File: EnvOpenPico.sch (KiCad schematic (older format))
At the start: 37 parts, among them J2 Conn_01x02, J3 Conn_02x18_Odd_Even, J4 Conn_02x18_Odd_Even, J5 Conn_01x03_Male, U1 SPX3819M5-L-3-3, U2 W25Q256JVEIQ, U3 RP2040, X1 XO32

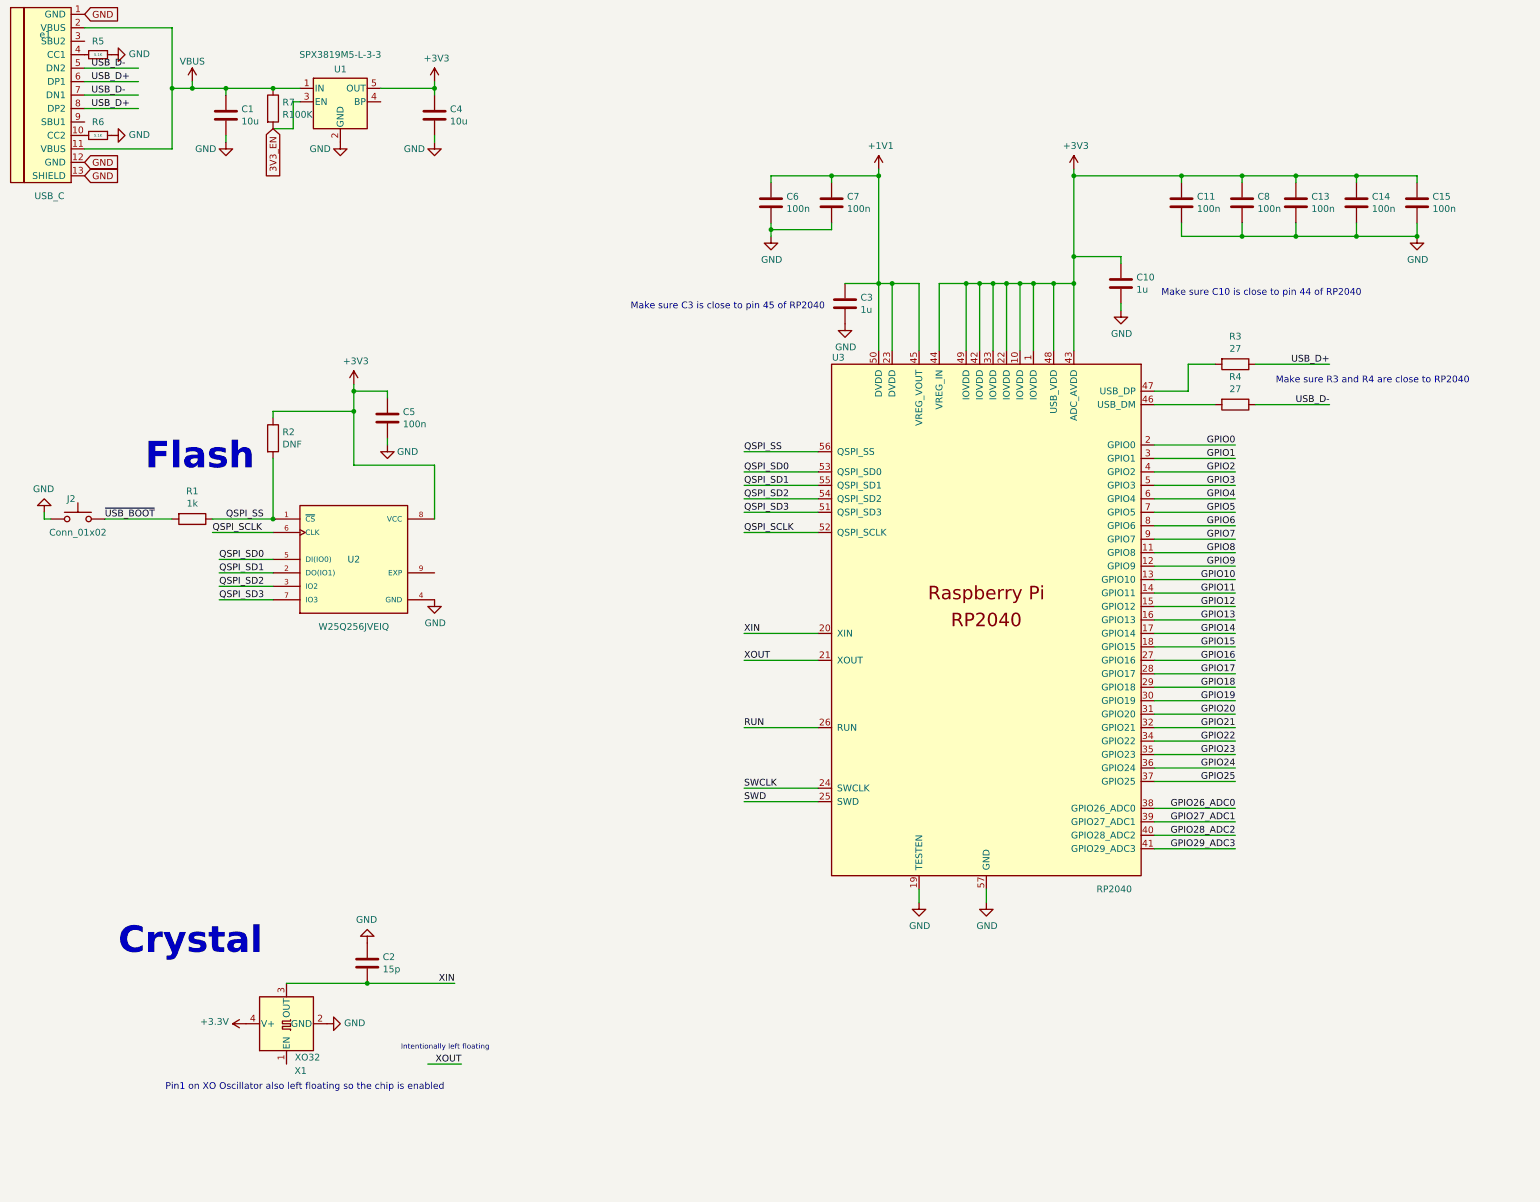
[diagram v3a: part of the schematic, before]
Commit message: Added a Bunch of notes and useful info to the schematic
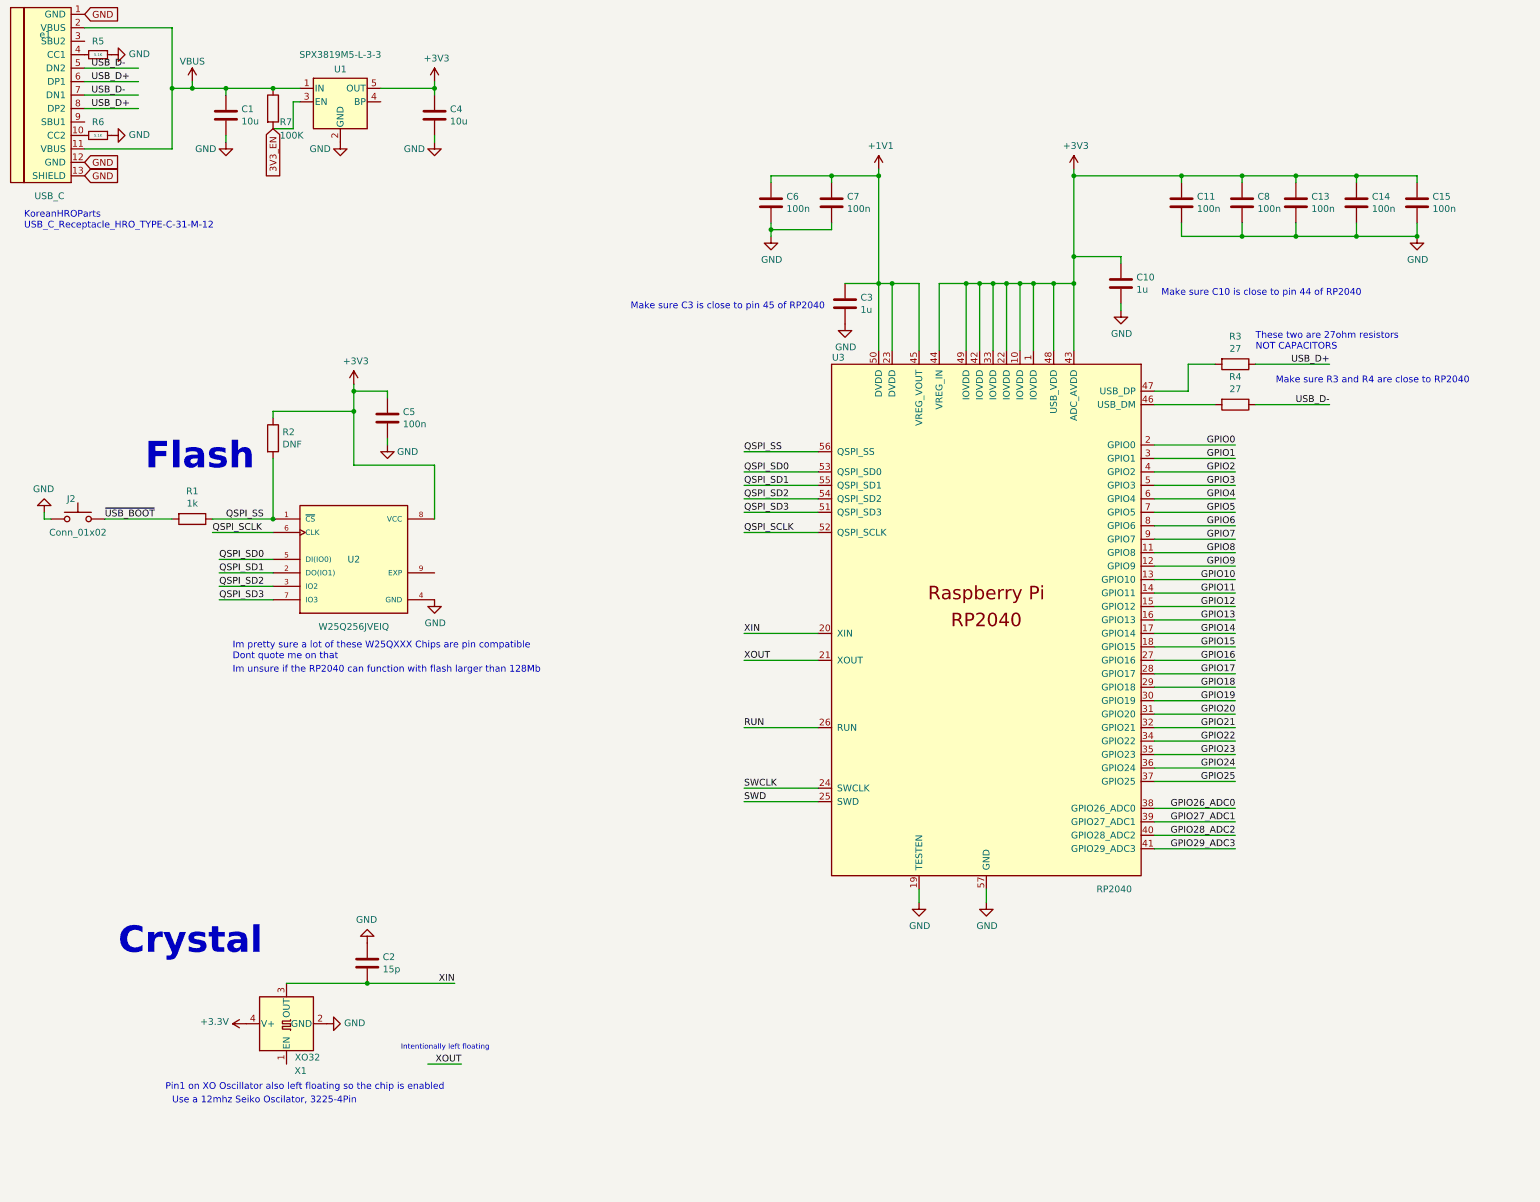
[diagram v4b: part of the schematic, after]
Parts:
- R7: value R100K -> 100K
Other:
- note added: "Im pretty sure a lot of these W25QXXX Chips are pin compatible\nDont quote me on that"
- note added: "Im unsure if the RP2040 can function with flash larger than 128Mb"
- note added: "KoreanHROParts \nUSB_C_Receptacle_HRO_TYPE-C-31-M-12"
- note added: "These two are 27ohm resistors \nNOT CAPACITORS"
- note added: "Use a 12mhz Seiko Oscilator, 3225-4Pin"
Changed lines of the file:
@@
 U 1 1 608CFAF0
 P 2500 1900
-F 0 "R7" H 2570 1946 50  0000 L CNN
-F 1 "R100K" H 2570 1855 50  0000 L CNN
+F 0 "R7" H 2550 1800 50  0000 L CNN
+F 1 "100K" H 2550 1700 50  0000 L CNN
 F 2 "Resistor_SMD:R_0402_1005Metric" V 2430 1900 50  0001 C CNN
 F 3 "~" H 2500 1900 50  0001 C CNN
@@
 	1    0    0    -1
 $EndComp
+Text Notes 1750 9300 0    50   ~ 0
+Use a 12mhz Seiko Oscilator, 3225-4Pin
+Text Notes 2200 6000 0    50   ~ 0
+Im pretty sure a lot of these W25QXXX Chips are pin compatible\nDont quote me on that
+Text Notes 9800 3700 0    50   ~ 0
+These two are 27ohm resistors \nNOT CAPACITORS
+Text Notes 650  2800 0    50   ~ 0
+KoreanHROParts \nUSB_C_Receptacle_HRO_TYPE-C-31-M-12
+Text Notes 2200 6100 0    50   ~ 0
+Im unsure if the RP2040 can function with flash larger than 128Mb
 $EndSCHEMATC

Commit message: Added some more notes
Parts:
- R8: value R470 -> 470
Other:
- note added: "2x 5.1K Resistors on the CC pins will = 5V@1.5A\nthis is the recomended default config for type-c"
- note added: "Dont bother trying to use a crystal\nas it massively complicates this clock source setup"
- note added: "Pin 9 technically doesnt exist\nits the main central contact under\nthe chip for heat dicipation"
- note added: "Pin1 on XO Oscillator also left floating so the chip is enabled\n(this is specified in their datasheet)"
- note added: "These decoupling capacitors are meant\nto be put close by each 3.3V pin of the RP2040"
- note removed: "Pin1 on XO Oscillator also left floating so the chip is enabled"
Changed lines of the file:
@@
 U 1 1 5EDB7D8D
 P 1000 1750
-F 0 "e1" H 850 2150 50  0000 R CNN
+F 0 "e1" H 750 2150 50  0000 R CNN
 F 1 "USB_C" H 950 950 50  0000 R CNN
 F 2 "Connector_USB:USB_C_Receptacle_HRO_TYPE-C-31-M-12" H 1150 1700 50  0001 C CNN
@@
 P 14500 7600
 F 0 "R8" V 14293 7600 50  0000 C CNN
-F 1 "R470" V 14384 7600 50  0000 C CNN
+F 1 "470" V 14384 7600 50  0000 C CNN
 F 2 "Resistor_SMD:R_0402_1005Metric" V 14430 7600 50  0001 C CNN
 F 3 "~" H 14500 7600 50  0001 C CNN
@@
 Text Notes 3450 8900 0    39   ~ 0
 Intentionally left floating
-Text Notes 1700 9200 0    50   ~ 0
-Pin1 on XO Oscillator also left floating so the chip is enabled
+Text Notes 1700 9250 0    50   ~ 0
+Pin1 on XO Oscillator also left floating so the chip is enabled\n(this is specified in their datasheet)
 Wire Wire Line
 	7000 2400 7000 3200
@@
 P 2500 1900
 F 0 "R7" H 2550 1800 50  0000 L CNN
-F 1 "100K" H 2550 1700 50  0000 L CNN
+F 1 "100K" V 2500 1850 30  0000 L CNN
 F 2 "Resistor_SMD:R_0402_1005Metric" V 2430 1900 50  0001 C CNN
 F 3 "~" H 2500 1900 50  0001 C CNN
@@
 	1    0    0    -1
 $EndComp
-Text Notes 1750 9300 0    50   ~ 0
+Text Notes 1700 9350 0    50   ~ 0
 Use a 12mhz Seiko Oscilator, 3225-4Pin
 Text Notes 2200 6000 0    50   ~ 0
@@
 Text Notes 2200 6100 0    50   ~ 0
 Im unsure if the RP2040 can function with flash larger than 128Mb
+Text Notes 3550 5250 0    50   ~ 0
+Pin 9 technically doesnt exist\nits the main central contact under\nthe chip for heat dicipation
+Text Notes 3200 8650 0    50   ~ 0
+Dont bother trying to use a crystal\nas it massively complicates this clock source setup
+Text Notes 9300 2350 0    50   ~ 0
+These decoupling capacitors are meant\nto be put close by each 3.3V pin of the RP2040
+Text Notes 1800 1350 0    50   ~ 0
+2x 5.1K Resistors on the CC pins will = 5V@1.5A\nthis is the recomended default config for type-c
 $EndSCHEMATC

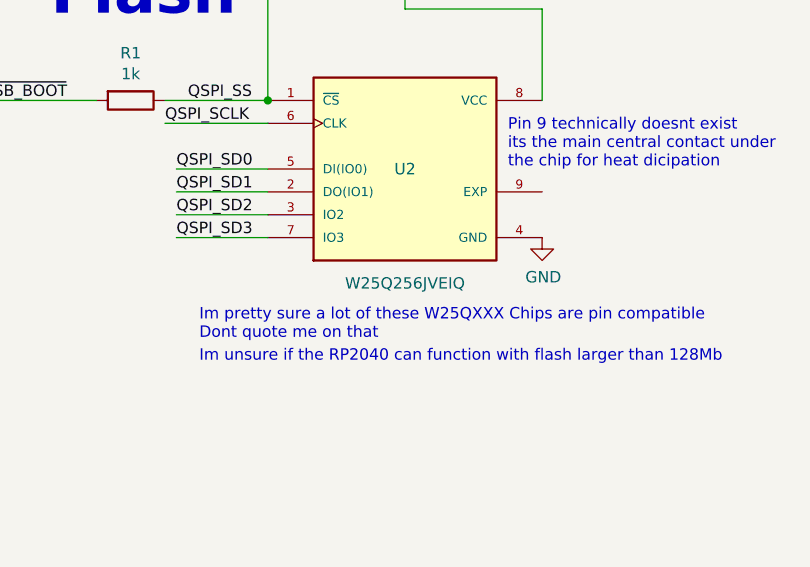
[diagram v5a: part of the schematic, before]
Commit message: Changed flash part number for a compatible version incase JLC has stock
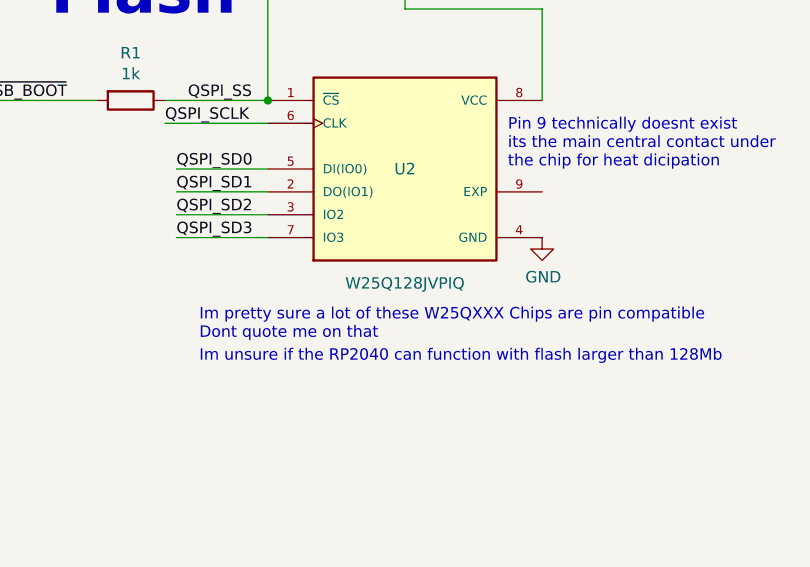
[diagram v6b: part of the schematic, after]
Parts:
- U2: value W25Q256JVEIQ -> W25Q128JVPIQ
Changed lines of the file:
@@
 P 3100 5250
 F 0 "U2" H 3100 5250 50  0000 C CNN
-F 1 "W25Q256JVEIQ" H 3100 4750 50  0000 C CNN
+F 1 "W25Q128JVPIQ" H 3100 4750 50  0000 C CNN
 F 2 "" H 3100 5250 50  0001 L BNN
 F 3 "" H 3100 5250 50  0001 L BNN

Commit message: Some general changes and house keeping
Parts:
- D2: value D_Schottky -> 0603 Diode; footprint Diode_SMD:D_0603_1608Metric -> Diode_SMD:D_0603_1608Metri
- D3: value GPIO25 LED -> LED 0402
- X1: value XO32 -> XO 32 12Mhz
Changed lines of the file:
@@
 P 14450 5100
 F 0 "D2" H 15000 4900 50  0000 C CNN
-F 1 "D_Schottky" H 14850 5000 50  0000 C CNN
-F 2 "Diode_SMD:D_0603_1608Metric" H 14450 5100 50  0001 C CNN
+F 1 "0603 Diode" H 14850 5000 50  0000 C CNN
+F 2 "Diode_SMD:D_0603_1608Metri" H 14450 5100 50  0001 C CNN
 F 3 "~" H 14450 5100 50  0001 C CNN
 	1    14450 5100
@@
 P 14800 7600
 F 0 "D3" H 14750 7350 50  0000 C CNN
-F 1 "GPIO25 LED" H 14600 7450 50  0000 C CNN
+F 1 "LED 0402" H 14600 7450 50  0000 C CNN
 F 2 "LED_SMD:LED_0402_1005Metric" H 14800 7600 50  0001 C CNN
 F 3 "~" H 14800 7600 50  0001 C CNN
@@
 P 2600 8700
 F 0 "X1" V 2250 8550 50  0000 L CNN
-F 1 "XO32" V 2350 8450 50  0000 L CNN
+F 1 "XO 32 12Mhz" V 2350 8450 50  0000 L CNN
 F 2 "Crystal:Crystal_SMD_SeikoEpson_TSX3225-4Pin_3.2x2.5mm" H 3300 8350 50  0001 C CNN
 F 3 "http://cdn-reichelt.de/documents/datenblatt/B400/XO32.pdf" H 2500 8700 50  0001 C CNN

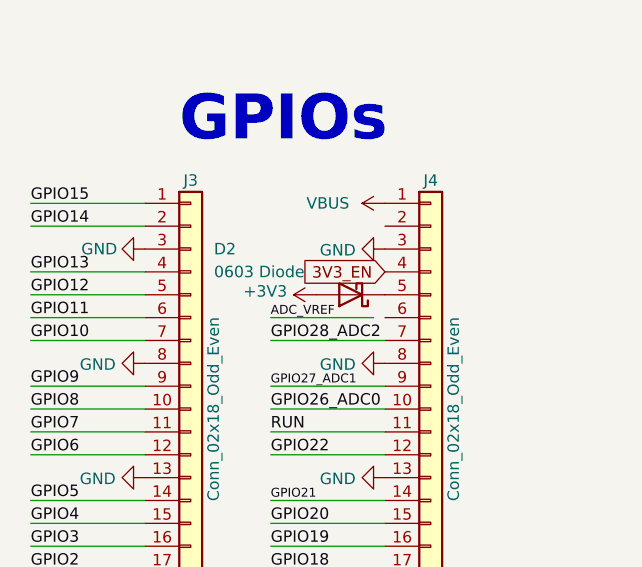
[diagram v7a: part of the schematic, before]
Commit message: some silkscreen adjustments and a couple added notes to schematic
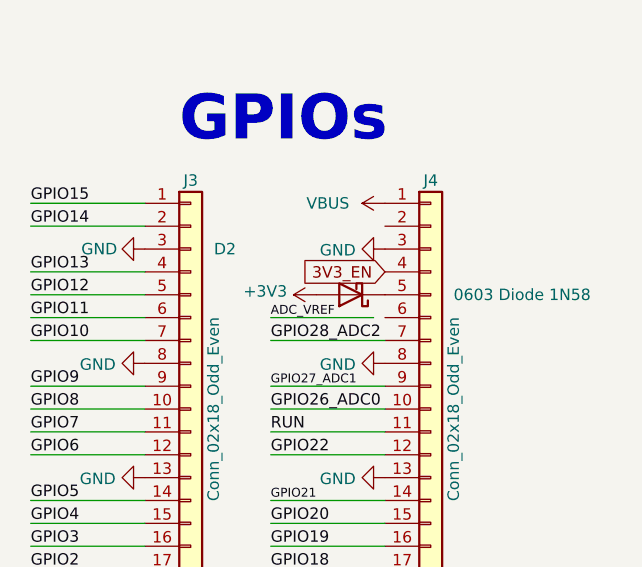
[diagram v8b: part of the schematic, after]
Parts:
- D2: value 0603 Diode -> 0603 Diode 1N58
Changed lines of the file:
@@
 P 14450 5100
 F 0 "D2" H 15000 4900 50  0000 C CNN
-F 1 "0603 Diode" H 14850 5000 50  0000 C CNN
+F 1 "0603 Diode 1N58" H 13700 5100 50  0000 C CNN
 F 2 "Diode_SMD:D_0603_1608Metri" H 14450 5100 50  0001 C CNN
 F 3 "~" H 14450 5100 50  0001 C CNN
